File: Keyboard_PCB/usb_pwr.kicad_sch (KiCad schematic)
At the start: 50 parts, among them J2 USB-C 16P, U2 USBLC6-2SC6, U5 MCP73871, U6 MCP73871

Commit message: Power section finished
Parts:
- R20, R21: value 180k -> 10k
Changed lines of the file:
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@@
 		)
 	)
+	(text_box "| stat[1,2], nPG | MODE                                |\n|----------------|-------------------------------------|\n| 0, 0, 0        | fault (temp | timer)                |\n| 0, 1, 0        | pre_cond, const current/volt        |\n| 0, 1, 1        | battery low                         |\n| 1, 0, 0        | stadby (charge complete)            |\n| 1, 1, 0        | shutdown (Vout=Vin | CE=0 | no bat) |\n| 1, 1, 1        | shutdown (Vout=Vbat | no power)     |\n"
+		(exclude_from_sim no)
+		(at 105.41 105.41 0)
+		(size 62.23 18.415)
+		(stroke
+			(width 0)
+			(type default)
+		)
+		(fill
+			(type none)
+		)
+		(effects
+			(font
+				(face "Andale Mono")
+				(size 1.27 1.27)
+			)
+			(justify left top)
+		)
+	)
 	(text "USB"
 		(exclude_from_sim no)
@@
 			)
 		)
-		(property "Value" "180k"
+		(property "Value" "10k"
 			(at 19.812 161.29 90)
 			(effects
@@
 			)
 		)
-		(property "Value" "180k"
+		(property "Value" "10k"
 			(at 21.082 104.14 90)
 			(effects

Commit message: Progress
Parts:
- added C31, C32: 10u, Capacitor_SMD:C_0603_1608Metric, symbol Device:C_Small
- added C33, C34: 4u7, Capacitor_SMD:C_0603_1608Metric, symbol Device:C_Small
- added D3: 5V, symbol Device:D_Zener_Small
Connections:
- net +5V: now also U5.17 (CE), U5.9 (~{TE}), U6.17 (CE), U6.9 (~{TE}), C31.1, C32.1, D3.1 (K)
- net GND: now also C31.2, C32.2, C33.2, C34.2, D3.2 (A)
- net VIN: now also C33.1, C34.1
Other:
- moved on the sheet: R20, R21

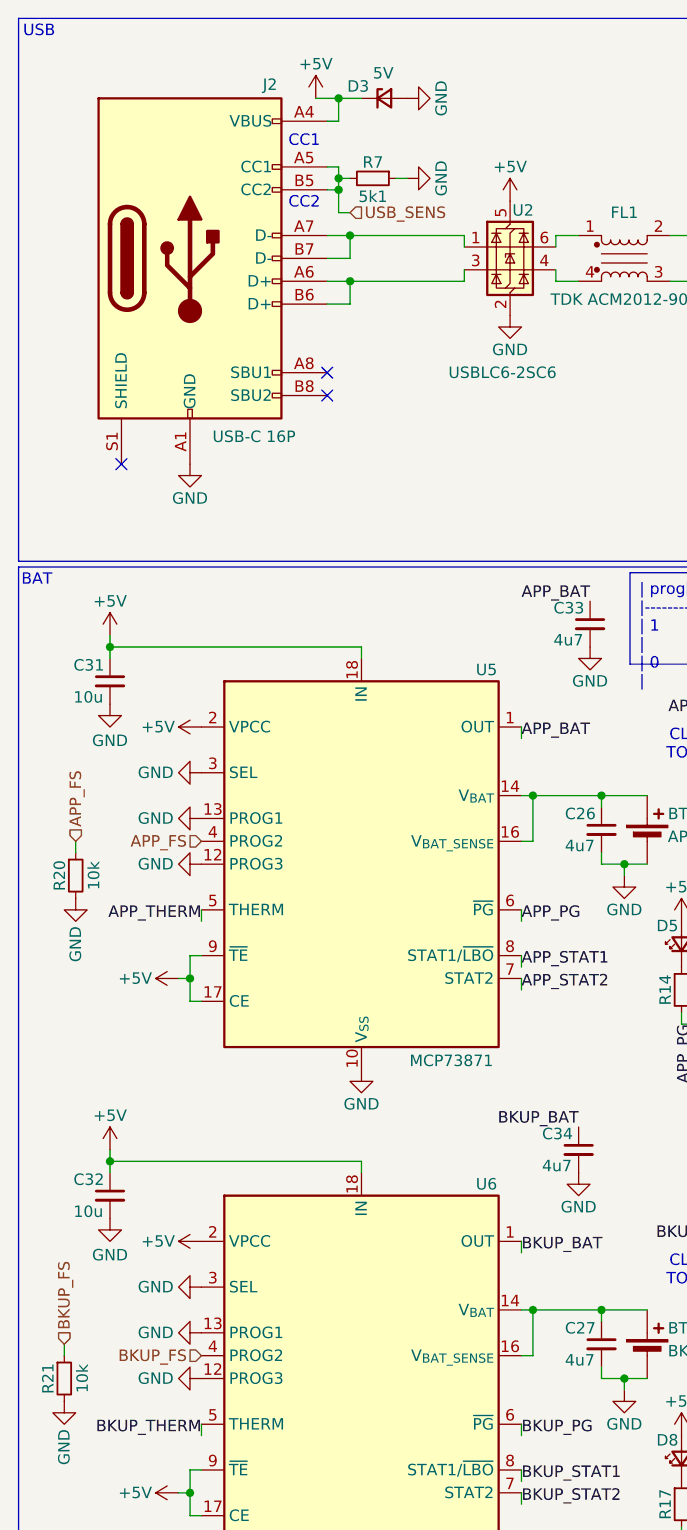
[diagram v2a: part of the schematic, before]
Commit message: Footprint assignments
TODO: check FPC connector
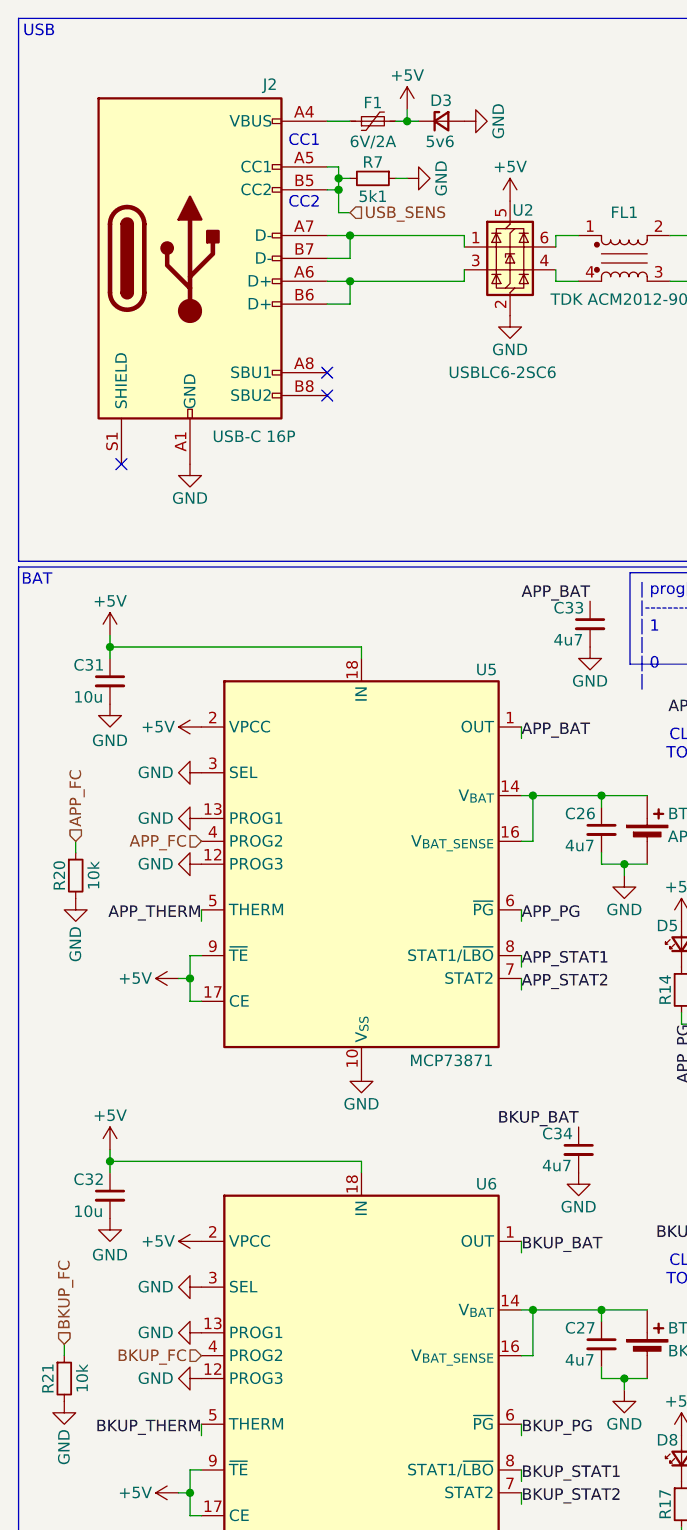
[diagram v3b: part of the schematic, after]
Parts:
- added F1: 6V/2A, Fuse:Fuse_1206_3216Metric, symbol Device:Polyfuse_Small
- BT1, BT2: footprint (none) -> Connector_PinHeader_2.54mm:PinHeader_1x02_P2.54mm_Vertical
- D10, D5, D6, D7, D8, D9: footprint (none) -> LED_SMD:LED_0603_1608Metric
- D3: value 5V -> 5v6; footprint (none) -> Diode_SMD:D_SOD-123
- L2, L3: footprint (none) -> Inductor_SMD:L_0805_2012Metric
- TH1, TH2: footprint (none) -> Resistor_SMD:R_0603_1608Metric
- TP1: footprint (none) -> TestPoint:TestPoint_Loop_D2.54mm_Drill1.5mm_Beaded
- TP2: footprint (none) -> TestPoint:TestPoint_Loop_D2.60mm_Drill0.9mm_Beaded
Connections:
- net +5V: now also F1.2; no longer J2.A4 (VBUS), J2.A9 (VBUS), J2.B4 (VBUS), J2.B9 (VBUS)
- net APP_FS renamed APP_FC
- net BKUP_FS renamed BKUP_FC
- new net: F1.1, J2.A4 (VBUS), J2.A9 (VBUS), J2.B4 (VBUS), J2.B9 (VBUS)
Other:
- moved on the sheet: D3
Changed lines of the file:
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@@
 	)
 	(junction
-		(at 48.26 21.59)
+		(at 128.27 82.55)
 		(diameter 0)
 		(color 0 0 0 0)
 	)
 	(junction
-		(at 128.27 82.55)
+		(at 161.29 34.29)
 		(diameter 0)
 		(color 0 0 0 0)
 	)
 	(junction
-		(at 161.29 34.29)
+		(at 168.91 34.29)
 		(diameter 0)
 		(color 0 0 0 0)
 	)
 	(junction
-		(at 168.91 34.29)
+		(at 55.88 24.13)
 		(diameter 0)
 		(color 0 0 0 0)
@@
 	(wire
 		(pts
-			(xy 48.26 21.59) (xy 48.26 24.13)
+			(xy 49.53 39.37) (xy 49.53 36.83)
 		)
 		(stroke
@@
 	(wire
 		(pts
-			(xy 49.53 39.37) (xy 49.53 36.83)
+			(xy 119.38 77.47) (xy 119.38 76.2)
 		)
 		(stroke
@@
 	(wire
 		(pts
-			(xy 119.38 77.47) (xy 119.38 76.2)
+			(xy 31.75 121.92) (xy 33.02 121.92)
 		)
 		(stroke
@@
 	(wire
 		(pts
-			(xy 31.75 121.92) (xy 33.02 121.92)
+			(xy 54.61 24.13) (xy 55.88 24.13)
 		)
 		(stroke
@@
 	(wire
 		(pts
+			(xy 46.99 24.13) (xy 49.53 24.13)
+		)
+		(stroke
+			(width 0)
+			(type default)
+		)
+	)
+	(wire
+		(pts
 			(xy 68.58 156.21) (xy 69.85 156.21)
 		)
@@
 	(wire
 		(pts
-			(xy 48.26 24.13) (xy 46.99 24.13)
-		)
-		(stroke
-			(width 0)
-			(type default)
-		)
-	)
-	(wire
-		(pts
 			(xy 49.53 34.29) (xy 48.26 34.29)
 		)
@@
 	(wire
 		(pts
-			(xy 45.72 21.59) (xy 48.26 21.59)
-		)
-		(stroke
-			(width 0)
-			(type default)
-		)
-	)
-	(wire
-		(pts
 			(xy 33.02 116.84) (xy 31.75 116.84)
 		)
@@
 	(wire
 		(pts
-			(xy 48.26 21.59) (xy 50.8 21.59)
+			(xy 55.88 24.13) (xy 57.15 24.13)
 		)
 		(stroke
@@
 	(wire
 		(pts
+			(xy 55.88 24.13) (xy 55.88 22.86)
+		)
+		(stroke
+			(width 0)
+			(type default)
+		)
+	)
+	(wire
+		(pts
 			(xy 68.58 92.71) (xy 68.58 91.44)
 		)
@@
 		)
 	)
-	(hierarchical_label "APP_FS"
+	(hierarchical_label "APP_FC"
 		(shape input)
 		(at 33.02 104.14 180)
@@
 		)
 	)
-	(hierarchical_label "BKUP_FS"
+	(hierarchical_label "BKUP_FC"
 		(shape input)
 		(at 33.02 161.29 180)
@@
 		)
 	)
-	(hierarchical_label "APP_FS"
+	(hierarchical_label "APP_FC"
 		(shape input)
 		(at 19.05 104.14 90)
@@
 		)
 	)
-	(hierarchical_label "BKUP_FS"
+	(hierarchical_label "BKUP_FC"
 		(shape input)
 		(at 17.78 160.02 90)
@@
 			)
 		)
-		(property "Footprint" ""
+		(property "Footprint" "LED_SMD:LED_0603_1608Metric"
 			(at 92.71 115.57 90)
 			(effects
@@
 			)
 		)
-		(property "Footprint" ""
+		(property "Footprint" "Connector_PinHeader_2.54mm:PinHeader_1x02_P2.54mm_Vertical"
 			(at 82.55 159.766 90)
 			(effects
@@
 	(symbol
 		(lib_id "power:GND")
-		(at 55.88 21.59 90)
+		(at 62.23 24.13 90)
 		(unit 1)
 		(exclude_from_sim no)
@@
 		(dnp no)
 		(property "Reference" "#PWR085"
-			(at 62.23 21.59 0)
+			(at 68.58 24.13 0)
 			(effects
 				(font
@@
 		)
 		(property "Value" "GND"
-			(at 59.69 21.59 0)
+			(at 66.04 24.13 0)
 			(effects
 				(font
@@
 		)
 		(property "Footprint" ""
-			(at 55.88 21.59 0)
+			(at 62.23 24.13 0)
 			(effects
 				(font
@@
 		)
 		(property "Datasheet" ""
-			(at 55.88 21.59 0)
+			(at 62.23 24.13 0)
 			(effects
 				(font
@@
 		)
 		(property "Description" "Power symbol creates a global label with name \"GND\" , ground"
-			(at 55.88 21.59 0)
+			(at 62.23 24.13 0)
 			(effects
 				(font
@@
 			)
 		)
-		(property "Footprint" ""
+		(property "Footprint" "Resistor_SMD:R_0603_1608Metric"
 			(at 95.25 151.13 0)
 			(effects
@@
 			)
 		)
-		(property "Footprint" ""
+		(property "Footprint" "LED_SMD:LED_0603_1608Metric"
 			(at 86.36 172.72 90)
 			(effects
@@
 			)
 		)
-		(property "Footprint" ""
+		(property "Footprint" "TestPoint:TestPoint_Loop_D2.60mm_Drill0.9mm_Beaded"
 			(at 168.91 85.09 0)
 			(effects
@@
 	)
 	(symbol
+		(lib_id "Device:Polyfuse_Small")
+		(at 52.07 24.13 90)
+		(unit 1)
+		(exclude_from_sim no)
+		(in_bom yes)
+		(on_board yes)
+		(dnp no)
+		(property "Reference" "F1"
+			(at 52.07 22.098 90)
+			(effects
+				(font
+					(size 1.27 1.27)
+				)
+			)
+		)
+		(property "Value" "6V/2A"
+			(at 52.07 26.416 90)
+			(effects
+				(font
+					(size 1.27 1.27)
+				)
+			)
+		)
+		(property "Footprint" "Fuse:Fuse_1206_3216Metric"
+			(at 57.15 22.86 0)
+			(effects
+				(font
+					(size 1.27 1.27)
+				)
+				(justify left)
+				(hide yes)
+			)
+		)
+		(property "Datasheet" "~"
+			(at 52.07 24.13 0)
+			(effects
+				(font
+					(size 1.27 1.27)
+				)
+				(hide yes)
+			)
+		)
+		(property "Description" "Resettable fuse, polymeric positive temperature coefficient, small symbol"
+			(at 52.07 24.13 0)
+			(effects
+				(font
+					(size 1.27 1.27)
+				)
+				(hide yes)
+			)
+		)
+		(pin "1"
+		)
+		(pin "2"
+		)
+		(instances
+			(project ""
+				(path "/dd51e792-c76c-4d43-96de-494177f3b593/f183b390-0c59-4c65-8a55-408064b389c7"
+					(reference "F1")
+					(unit 1)
+				)
+			)
+		)
+	)
+	(symbol
 		(lib_id "Device:R_Small")
 		(at 153.67 80.01 0)
@@
 			)
 		)
-		(property "Footprint" ""
+		(property "Footprint" "TestPoint:TestPoint_Loop_D2.54mm_Drill1.5mm_Beaded"
 			(at 168.91 43.18 0)
 			(effects
@@
 			)
 		)
-		(property "Footprint" ""
+		(property "Footprint" "Inductor_SMD:L_0805_2012Metric"
 			(at 139.7 25.4 0)
 			(effects
@@
 			)
 		)
-		(property "Footprint" ""
+		(property "Footprint" "LED_SMD:LED_0603_1608Metric"
 			(at 99.06 115.57 90)
 			(effects
@@
 			)
 		)
-		(property "Footprint" ""
+		(property "Footprint" "LED_SMD:LED_0603_1608Metric"
 			(at 86.36 115.57 90)
 			(effects
@@
 	(symbol
 		(lib_id "Device:D_Zener_Small")
-		(at 53.34 21.59 0)
+		(at 59.69 24.13 0)
 		(unit 1)
 		(exclude_from_sim no)
@@
 		(dnp no)
 		(property "Reference" "D3"
-			(at 49.2125 20.2565 0)
+			(at 58.42 21.844 0)
 			(effects
 				(font
@@
 			)
 		)
-		(property "Value" "5V"
-			(at 52.07 18.796 0)
+		(property "Value" "5v6"
+			(at 57.912 26.416 0)
 			(effects
 				(font
@@
 			)
 		)
-		(property "Footprint" ""
-			(at 53.34 21.59 90)
+		(property "Footprint" "Diode_SMD:D_SOD-123"
+			(at 59.69 24.13 90)
 			(effects
 				(font
@@
 		)
 		(property "Datasheet" "~"
-			(at 53.34 21.59 90)
+			(at 59.69 24.13 90)
 			(effects
 				(font
@@
 		)
 		(property "Description" "Zener diode, small symbol"
-			(at 53.34 21.59 0)
+			(at 59.69 24.13 0)
 			(effects
 				(font
@@
 			)
 		)
-		(property "Footprint" ""
+		(property "Footprint" "Connector_PinHeader_2.54mm:PinHeader_1x02_P2.54mm_Vertical"
 			(at 82.55 102.616 90)
 			(effects
@@
 			)
 		)
-		(property "Footprint" ""
+		(property "Footprint" "LED_SMD:LED_0603_1608Metric"
 			(at 92.71 172.72 90)
 			(effects
@@
 			)
 		)
-		(property "Footprint" ""
+		(property "Footprint" "Inductor_SMD:L_0805_2012Metric"
 			(at 139.7 67.31 0)
 			(effects
@@
 			)
 		)
-		(property "Footprint" ""
+		(property "Footprint" "LED_SMD:LED_0603_1608Metric"
 			(at 99.06 172.72 90)
 			(effects
@@
 			)
 		)
-		(property "Footprint" ""
+		(property "Footprint" "Resistor_SMD:R_0603_1608Metric"
 			(at 95.25 92.71 0)
 			(effects
@@
 	(symbol
 		(lib_id "power:+5V")
-		(at 45.72 21.59 0)
+		(at 55.88 22.86 0)
 		(unit 1)
 		(exclude_from_sim no)
@@
 		(dnp no)
 		(property "Reference" "#PWR086"
-			(at 45.72 25.4 0)
+			(at 55.88 26.67 0)
 			(effects
 				(font
@@
 		)
 		(property "Value" "+5V"
-			(at 45.72 17.78 0)
+			(at 55.88 19.05 0)
 			(effects
 				(font
@@
 		)
 		(property "Footprint" ""
-			(at 45.72 21.59 0)
+			(at 55.88 22.86 0)
 			(effects
 				(font
@@
 		)
 		(property "Datasheet" ""
-			(at 45.72 21.59 0)
+			(at 55.88 22.86 0)
 			(effects
 				(font
@@
 		)
 		(property "Description" "Power symbol creates a global label with name \"+5V\""
-			(at 45.72 21.59 0)
+			(at 55.88 22.86 0)
 			(effects
 				(font

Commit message: Layout progress
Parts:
- added JP2: BAT_BYP, Jumper:SolderJumper-2_P1.3mm_Open_TrianglePad1.0x1.5mm, symbol Jumper:SolderJumper_2_Open
- D3: value 5v6 -> 5v1
- TP1: footprint TestPoint:TestPoint_Loop_D2.54mm_Drill1.5mm_Beaded -> TestPoint:TestPoint_Pad_D1.0mm
- TP2: footprint TestPoint:TestPoint_Loop_D2.60mm_Drill0.9mm_Beaded -> TestPoint:TestPoint_Pad_D1.0mm
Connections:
- net +5V: now also JP2.2 (B)
- net VIN: no longer C14.1, C15.1, C33.1, U3.10 (VIN), U3.11 (VIN), U5.1 (OUT), U5.20 (OUT)
- new net V_IN: C14.1, C15.1, C33.1, JP2.1 (A), U3.10 (V_IN), U3.11 (V_IN), U5.1 (OUT), U5.20 (OUT)
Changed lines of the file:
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@@
 	)
 	(junction
+		(at 124.46 34.29)
+		(diameter 0)
+		(color 0 0 0 0)
+	)
+	(junction
 		(at 165.1 76.2)
 		(diameter 0)
@@
 	)
 	(junction
-		(at 124.46 34.29)
-		(diameter 0)
-		(color 0 0 0 0)
-	)
-	(junction
 		(at 77.47 99.06)
 		(diameter 0)
@@
 	(wire
 		(pts
-			(xy 143.51 25.4) (xy 143.51 26.67)
+			(xy 46.99 39.37) (xy 49.53 39.37)
 		)
 		(stroke
@@
 	(wire
 		(pts
-			(xy 46.99 39.37) (xy 49.53 39.37)
+			(xy 124.46 34.29) (xy 130.81 34.29)
 		)
 		(stroke
@@
 	(wire
 		(pts
+			(xy 135.89 26.67) (xy 135.89 25.4)
+		)
+		(stroke
+			(width 0)
+			(type default)
+		)
+	)
+	(wire
+		(pts
 			(xy 72.39 40.64) (xy 72.39 41.91)
 		)
@@
 	(wire
 		(pts
-			(xy 77.47 163.83) (xy 80.01 163.83)
+			(xy 143.51 26.67) (xy 143.51 25.4)
 		)
 		(stroke
@@
 	(wire
 		(pts
-			(xy 93.98 181.61) (xy 92.71 181.61)
+			(xy 77.47 163.83) (xy 80.01 163.83)
 		)
 		(stroke
@@
 	(wire
 		(pts
-			(xy 130.81 34.29) (xy 124.46 34.29)
+			(xy 93.98 181.61) (xy 92.71 181.61)
 		)
 		(stroke
@@
 	(wire
 		(pts
-			(xy 135.89 26.67) (xy 135.89 25.4)
-		)
-		(stroke
-			(width 0)
-			(type default)
-		)
-	)
-	(wire
-		(pts
 			(xy 62.23 36.83) (xy 62.23 38.1)
 		)
@@
 	(wire
 		(pts
-			(xy 124.46 34.29) (xy 120.65 34.29)
+			(xy 120.65 34.29) (xy 124.46 34.29)
 		)
 		(stroke
@@
 			)
 		)
-		(property "Datasheet" ""
+		(property "Datasheet" "https://www.ti.com/lit/ds/symlink/tps63020.pdf?ts=1728564305031&ref_url=https%253A%252F%252Fwww.ti.com%252Fsitesearch%252Fen-us%252Fdocs%252Funiversalsearch.tsp%253FlangPref%253Den-US%2526nr%253D14%2526searchTerm%253DTPS63020DSJR"
 			(at 139.7 83.82 0)
 			(effects
@@
 	)
 	(symbol
+		(lib_id "Jumper:SolderJumper_2_Open")
+		(at 120.65 30.48 90)
+		(unit 1)
+		(exclude_from_sim yes)
+		(in_bom no)
+		(on_board yes)
+		(dnp no)
+		(property "Reference" "JP2"
+			(at 118.364 30.48 0)
+			(effects
+				(font
+					(size 1.27 1.27)
+				)
+			)
+		)
+		(property "Value" "BAT_BYP"
+			(at 126.492 30.48 90)
+			(effects
+				(font
+					(size 1.27 1.27)
+				)
+			)
+		)
+		(property "Footprint" "Jumper:SolderJumper-2_P1.3mm_Open_TrianglePad1.0x1.5mm"
+			(at 120.65 30.48 0)
+			(effects
+				(font
+					(size 1.27 1.27)
+				)
+				(hide yes)
+			)
+		)
+		(property "Datasheet" "~"
+			(at 120.65 30.48 0)
+			(effects
+				(font
+					(size 1.27 1.27)
+				)
+				(hide yes)
+			)
+		)
+		(property "Description" "Solder Jumper, 2-pole, open"
+			(at 120.65 30.48 0)
+			(effects
+				(font
+					(size 1.27 1.27)
+				)
+				(hide yes)
+			)
+		)
+		(pin "2"
+		)
+		(pin "1"
+		)
+		(instances
+			(project "Keyboard_PCB"
+				(path "/dd51e792-c76c-4d43-96de-494177f3b593/f183b390-0c59-4c65-8a55-408064b389c7"
+					(reference "JP2")
+					(unit 1)
+				)
+			)
+		)
+	)
+	(symbol
 		(lib_id "power:GND")
 		(at 124.46 82.55 0)
@@
 	)
 	(symbol
-		(lib_id "Marijn:TPS63020")
-		(at 139.7 41.91 0)
-		(unit 1)
-		(exclude_from_sim no)
-		(in_bom yes)
-		(on_board yes)
-		(dnp no)
-		(property "Reference" "U3"
-			(at 144.272 27.94 0)
-			(effects
-				(font
-					(size 1.27 1.27)
-				)
-				(justify left)
-			)
-		)
-		(property "Value" "~"
-			(at 145.7041 27.94 0)
-			(effects
-				(font
-					(size 1.27 1.27)
-				)
-				(justify left)
-			)
-		)
-		(property "Footprint" "Marijn_KiCad:QFN_DSJ"
-			(at 125.73 51.054 0)
-			(effects
-				(font
-					(size 1.27 1.27)
-				)
-				(hide yes)
-			)
-		)
-		(property "Datasheet" ""
-			(at 139.7 41.91 0)
-			(effects
-				(font
-					(size 1.27 1.27)
-				)
-				(hide yes)
-			)
-		)
-		(property "Description" ""
-			(at 139.7 41.91 0)
-			(effects
-				(font
-					(size 1.27 1.27)
-				)
-				(hide yes)
-			)
-		)
-		(pin "3"
-		)
-		(pin "9"
-		)
-		(pin "13"
-		)
-		(pin "4"
-		)
-		(pin "14"
-		)
-		(pin "7"
-		)
-		(pin "8"
-		)
-		(pin "6"
-		)
-		(pin "5"
-		)
-		(pin "2"
-		)
-		(pin "11"
-		)
-		(pin "15"
-		)
-		(pin "10"
-		)
-		(pin "12"
-		)
-		(pin "1"
-		)
-		(instances
-			(project "Keyboard_PCB"
-				(path "/dd51e792-c76c-4d43-96de-494177f3b593/f183b390-0c59-4c65-8a55-408064b389c7"
-					(reference "U3")
-					(unit 1)
-				)
-			)
-		)
-	)
-	(symbol
 		(lib_id "Connector:TestPoint")
 		(at 173.99 85.09 180)
@@
 			)
 		)
-		(property "Footprint" "TestPoint:TestPoint_Loop_D2.60mm_Drill0.9mm_Beaded"
+		(property "Footprint" "TestPoint:TestPoint_Pad_D1.0mm"
 			(at 168.91 85.09 0)
 			(effects
@@
 		)
 		(property "Value" "USBLC6-2SC6"
-			(at 60.452 52.07 0)
+			(at 60.452 51.562 0)
 			(effects
 				(font
@@
 			)
 		)
-		(property "Footprint" "TestPoint:TestPoint_Loop_D2.54mm_Drill1.5mm_Beaded"
+		(property "Footprint" "TestPoint:TestPoint_Pad_D1.0mm"
 			(at 168.91 43.18 0)
 			(effects
@@
 			)
 		)
-		(property "Value" "5v6"
+		(property "Value" "5v1"
 			(at 57.912 26.416 0)
 			(effects
@@
 	)
 	(symbol
+		(lib_name "TPS63020_1")
+		(lib_id "Marijn:TPS63020")
+		(at 139.7 41.91 0)
+		(unit 1)
+		(exclude_from_sim no)
+		(in_bom yes)
+		(on_board yes)
+		(dnp no)
+		(fields_autoplaced yes)
+		(property "Reference" "U3"
+			(at 145.7041 25.4 0)
+			(effects
+				(font
+					(size 1.27 1.27)
+				)
+				(justify left)
+			)
+		)
+		(property "Value" "~"
+			(at 145.7041 27.94 0)
+			(effects
+				(font
+					(size 1.27 1.27)
+				)
+				(justify left)
+			)
+		)
+		(property "Footprint" "Marijn_KiCad:QFN_DSJ"
+			(at 125.73 51.054 0)
+			(effects
+				(font
+					(size 1.27 1.27)
+				)
+				(hide yes)
+			)
+		)
+		(property "Datasheet" "https://www.ti.com/lit/ds/symlink/tps63020.pdf?ts=1728564305031&ref_url=https%253A%252F%252Fwww.ti.com%252Fsitesearch%252Fen-us%252Fdocs%252Funiversalsearch.tsp%253FlangPref%253Den-US%2526nr%253D14%2526searchTerm%253DTPS63020DSJR"
+			(at 142.748 52.832 0)
+			(effects
+				(font
+					(size 1.27 1.27)
+				)
+				(hide yes)
+			)
+		)
+		(property "Description" ""
+			(at 139.7 41.91 0)
+			(effects
+				(font
+					(size 1.27 1.27)
+				)
+				(hide yes)
+			)
+		)
+		(pin "14"
+		)
+		(pin "12"
+		)
+		(pin "13"
+		)
+		(pin "1"
+		)
+		(pin "5"
+		)
+		(pin "11"
+		)
+		(pin "4"
+		)
+		(pin "2"
+		)
+		(pin "10"
+		)
+		(pin "3"
+		)
+		(pin "7"
+		)
+		(pin "9"
+		)
+		(pin "15"
+		)
+		(pin "6"
+		)
+		(pin "8"
+		)
+		(instances
+			(project ""
+				(path "/dd51e792-c76c-4d43-96de-494177f3b593/f183b390-0c59-4c65-8a55-408064b389c7"
+					(reference "U3")
+					(unit 1)
+				)
+			)
+		)
+	)
+	(symbol
 		(lib_id "Device:C_Small")
 		(at 161.29 80.01 0)
@@
 					(unit 1)
 				)
+			)
+		)
+	)
+	(symbol
+		(lib_id "power:+5V")
+		(at 120.65 26.67 0)
+		(unit 1)
+		(exclude_from_sim no)
+		(in_bom yes)
+		(on_board yes)
+		(dnp no)
+		(property "Reference" "#PWR099"
+			(at 120.65 30.48 0)
+			(effects
+				(font
+					(size 1.27 1.27)
+				)
+				(hide yes)
+			)
+		)
+		(property "Value" "+5V"
+			(at 120.65 22.86 0)
+			(effects
+				(font
+					(size 1.27 1.27)
+				)
+			)
+		)
+		(property "Footprint" ""
+			(at 120.65 26.67 0)
+			(effects
+				(font
+					(size 1.27 1.27)
+				)
+				(hide yes)
+			)
+		)
+		(property "Datasheet" ""
+			(at 120.65 26.67 0)
+			(effects
+				(font
+					(size 1.27 1.27)
+				)
+				(hide yes)
+			)
+		)
+		(property "Description" "Power symbol creates a global label with name \"+5V\""
+			(at 120.65 26.67 0)
+			(effects
+				(font
+					(size 1.27 1.27)
+				)
+				(hide yes)
+			)
+		)
+		(pin "1"
+		)
+		(instances
+			(project "Keyboard_PCB"
+				(path "/dd51e792-c76c-4d43-96de-494177f3b593/f183b390-0c59-4c65-8a55-408064b389c7"
+					(reference "#PWR099")
+					(unit 1)
+				)
